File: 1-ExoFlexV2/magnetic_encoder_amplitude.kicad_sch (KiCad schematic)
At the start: 49 parts, among them J64 5,1k, J65 5,1k, J66 5,1k, J67 5,1k, J68 5,1k, J69 5,1k, U10 ADCMP602BRMZ, U11 SN74LVC1G32DBVR, U12 SN74LVC1G32DBVR, U8 ADCMP602BRMZ, U9 ADCMP602BRMZ

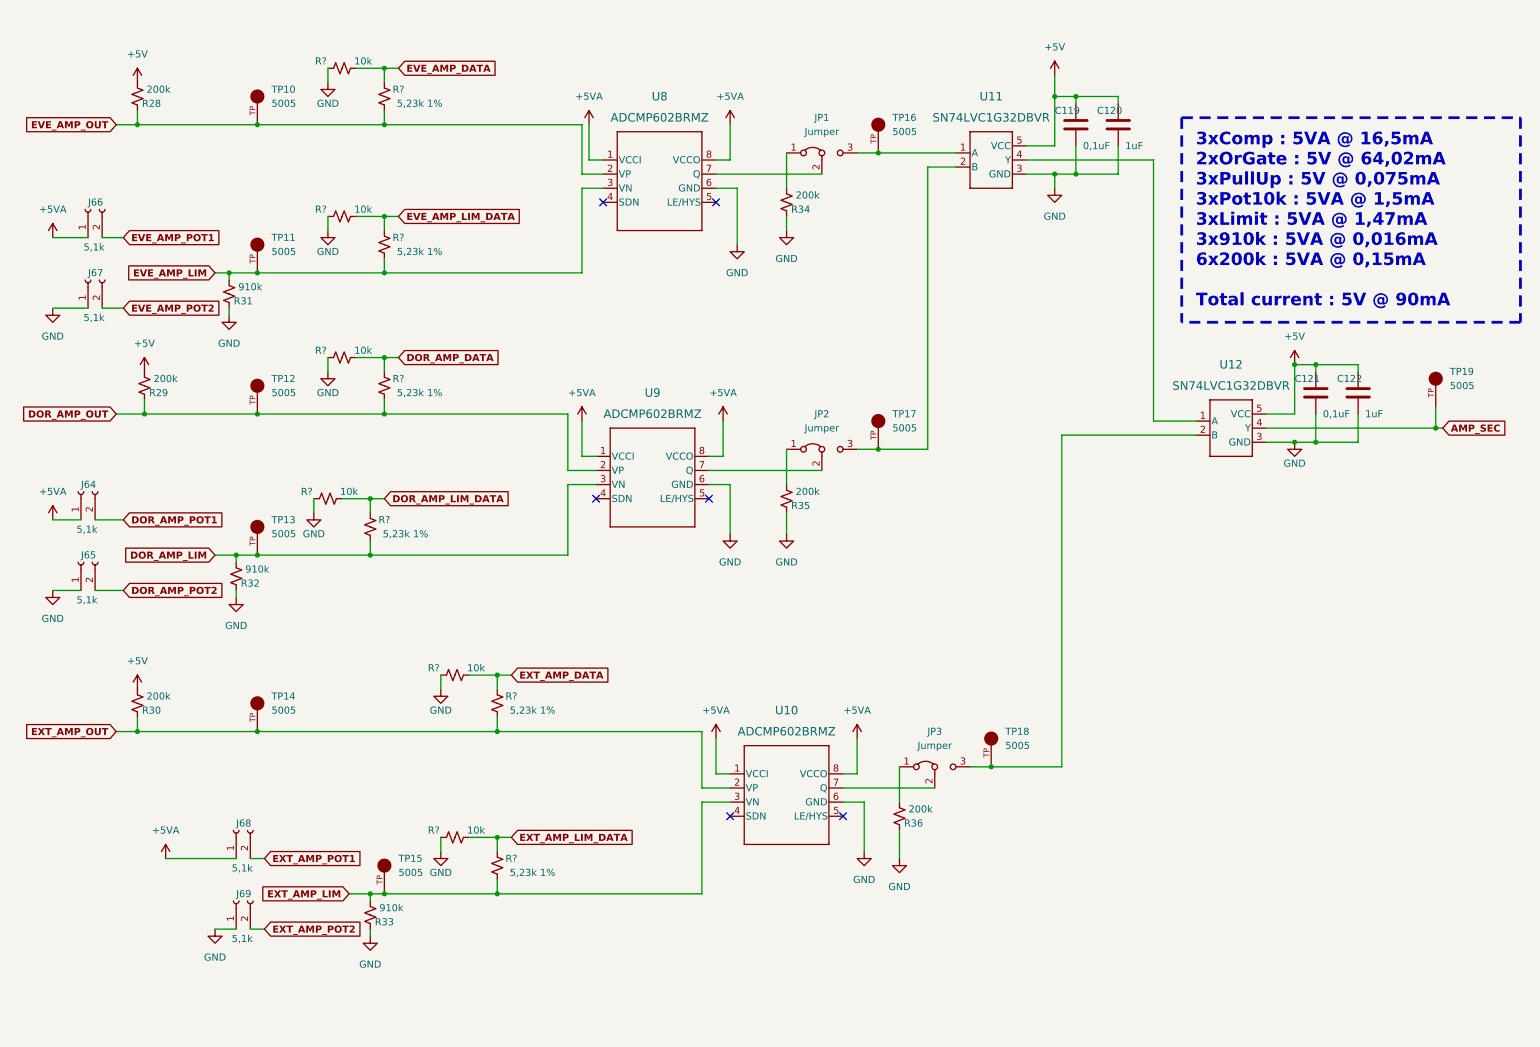
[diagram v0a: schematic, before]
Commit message: Finalisation 2
-Ajout des nouveaux comparateurs
- Ajout d'une page découplage
- Retrait des condensateur dans les autres pages
- Ajout de trimmer pour les résistance importante mais incertaines
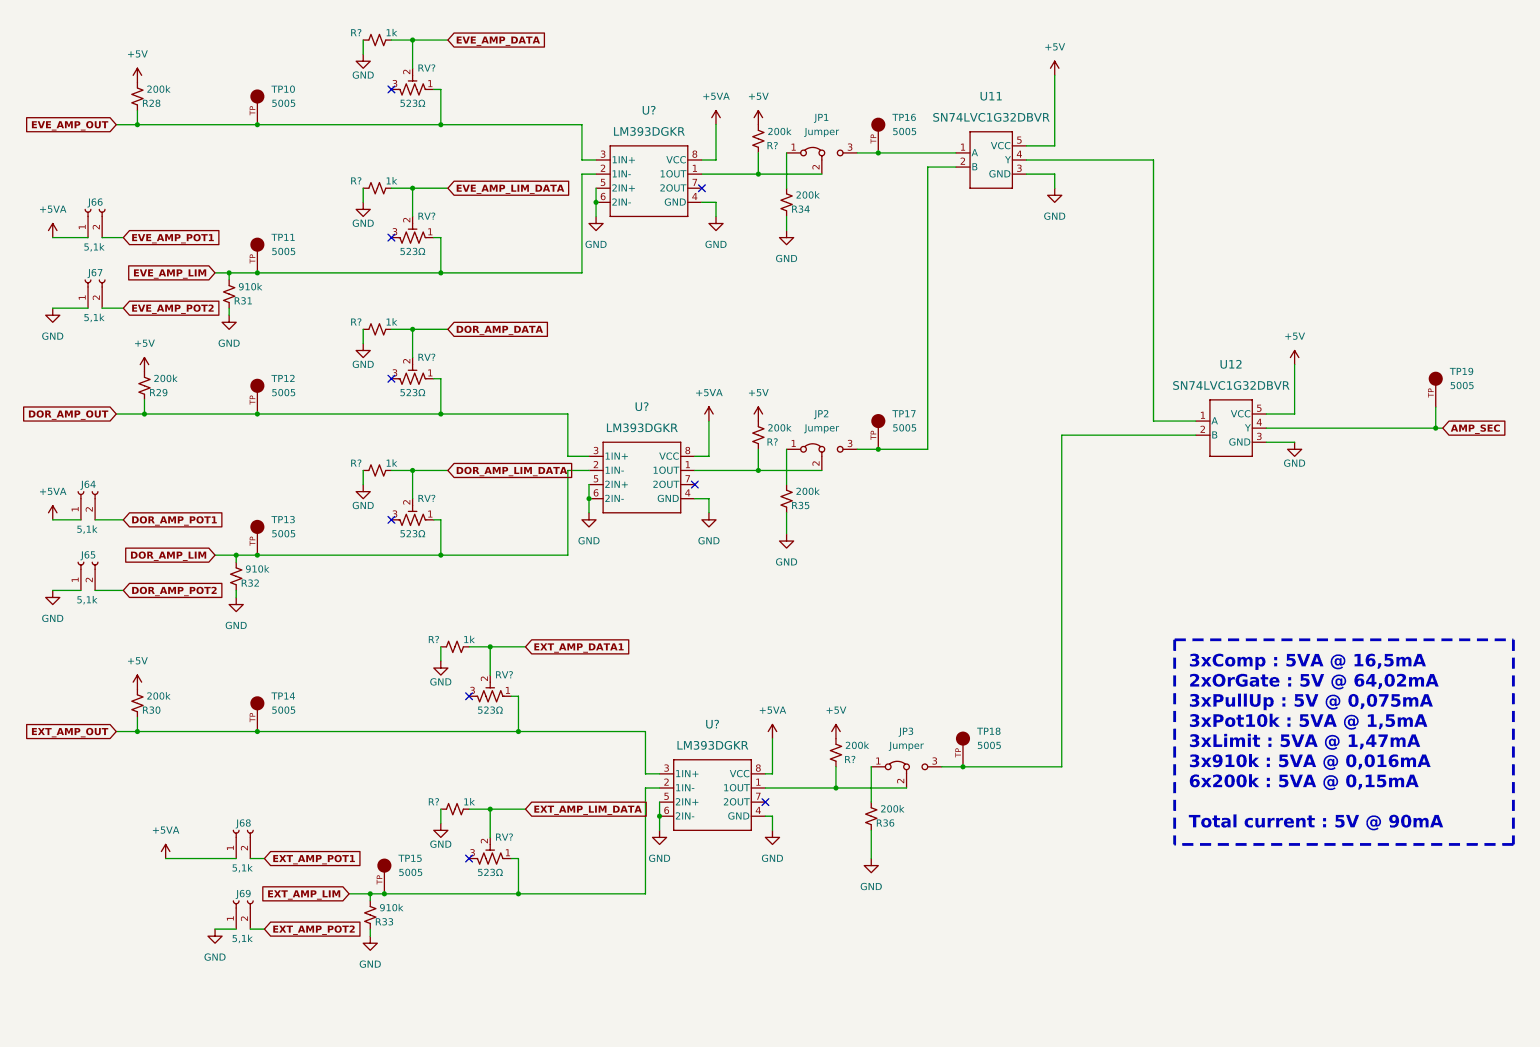
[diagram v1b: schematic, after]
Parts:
- removed C119, C121: 0,1uF, Capacitor_SMD:C_0603_1608Metric, symbol Device:C
- removed C120, C122: 1uF, Capacitor_SMD:C_0603_1608Metric, symbol Device:C
- removed R? (x6): 5,23k 1%, Resistor_SMD:R_0805_2012Metric, symbol Device:R_Small_US
- removed R? (x6): 10k, Resistor_SMD:R_0805_2012Metric, symbol Device:R_Small_US
- removed U10, U8, U9: ADCMP602BRMZ, FootPrint:ADCMP602BRMZ, symbol SymLib:ADCMP602BRMZ
- added R? (x3): 200k, Resistor_SMD:R_0603_1608Metric, symbol Device:R_Small_US
- added R? (x6): 1k, Resistor_SMD:R_0805_2012Metric, symbol Device:R_Small_US
- added RV? (x6): 523Ω, FootPrint:TRIM_3362P-1-102LF, symbol Device:R_Potentiometer_Trim_US
- added U? (x3): LM393DGKR, DGK8, symbol SymLib:LM393DGKR
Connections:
- net +5V: now also R?.1, R?.1, R?.1
- net +5VA: now also U?.8 (VCC), U?.8 (VCC), U?.8 (VCC)
- net DOR_AMP_DATA: now also R?.2, RV?.2
- net DOR_AMP_LIM: now also RV?.1, U?.2 (1IN-)
- net DOR_AMP_LIM_DATA: now also R?.2, RV?.2
- net DOR_AMP_OUT: now also RV?.1, U?.3 (1IN+)
- net EVE_AMP_DATA: now also R?.2, RV?.2
- net EVE_AMP_LIM: now also RV?.1, U?.2 (1IN-)
- net EVE_AMP_LIM_DATA: now also R?.2, RV?.2
- net EVE_AMP_OUT: now also RV?.1, U?.3 (1IN+)
- net EXT_AMP_LIM: now also RV?.1, U?.2 (1IN-)
- net EXT_AMP_LIM_DATA: now also R?.2, RV?.2
- net EXT_AMP_OUT: now also RV?.1, U?.3 (1IN+)
- net GND: now also R?.1, R?.1, R?.1, R?.1, R?.1, R?.1, U?.4 (GND), U?.4 (GND), U?.4 (GND), U?.5 (2IN+), U?.5 (2IN+), U?.5 (2IN+), U?.6 (2IN-), U?.6 (2IN-), U?.6 (2IN-)
- net at JP2.2 (C): now also R?.2, U?.1 (1OUT)
- net at JP1.2 (C): now also R?.2, U?.1 (1OUT)
- net at JP3.2 (C): now also R?.2, U?.1 (1OUT)
- new net EXT_AMP_DATA1: R?.2, RV?.2
- no-connect marks 6 -> 9
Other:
- moved on the sheet: JP3, R36, TP18

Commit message: Chokes et RC
- Ajout des RF chokes
- Changement des résistance pour 0805
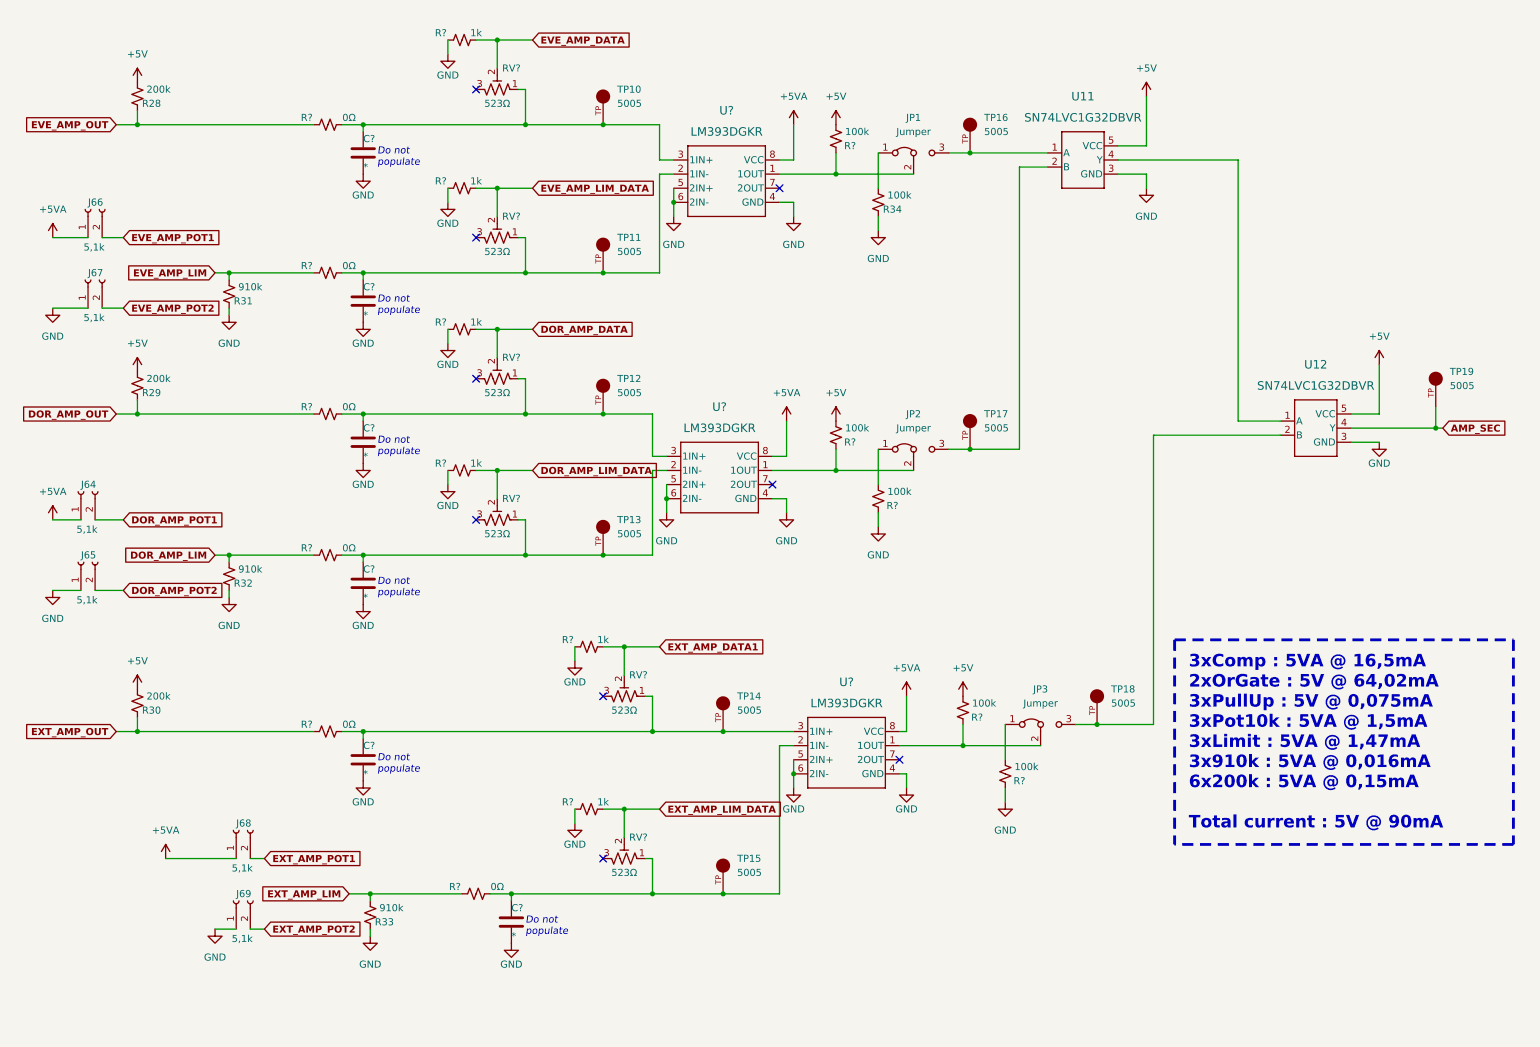
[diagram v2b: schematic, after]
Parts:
- removed R35, R36, R? (x2): 200k, Resistor_SMD:R_0603_1608Metric, symbol Device:R_Small_US
- added C? (x6): *, Capacitor_SMD:C_0805_2012Metric, symbol Device:C
- added R? (x4): 100k, Resistor_SMD:R_0805_2012Metric, symbol Device:R_Small_US
- added R? (x6): 0Ω, Resistor_SMD:R_0805_2012Metric, symbol Device:R_Small_US
- R28: footprint Resistor_SMD:R_0603_1608Metric -> Resistor_SMD:R_0805_2012Metric
- R34, R?: value 200k -> 100k; footprint Resistor_SMD:R_0603_1608Metric -> Resistor_SMD:R_0805_2012Metric
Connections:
- net +5V: now also R?.1, R?.1
- net DOR_AMP_LIM: now also R?.1; no longer RV?.1, TP13.TP, U?.2 (1IN-)
- net DOR_AMP_OUT: now also R?.1; no longer RV?.1, TP12.TP, U?.3 (1IN+)
- net EVE_AMP_LIM: now also R?.1; no longer RV?.1, TP11.TP, U?.2 (1IN-)
- net EVE_AMP_OUT: now also R?.1; no longer RV?.1, TP10.TP, U?.3 (1IN+)
- net EXT_AMP_LIM: now also R?.1; no longer RV?.1, TP15.TP, U?.2 (1IN-)
- net EXT_AMP_OUT: now also R?.1; no longer RV?.1, TP14.TP, U?.3 (1IN+)
- net GND: now also C?.2, C?.2, C?.2, C?.2, C?.2, C?.2, R?.2, R?.2
- net at JP3.2 (C), U?.1 (1OUT): now also R?.2
- net at JP2.1 (A): now also R?.1
- net at JP2.2 (C), U?.1 (1OUT): now also R?.2
- net at JP3.1 (A): now also R?.1
- new net: C?.1, R?.2, RV?.1, TP14.TP, U?.3 (1IN+)
- new net: C?.1, R?.2, RV?.1, TP10.TP, U?.3 (1IN+)
- new net: C?.1, R?.2, RV?.1, TP15.TP, U?.2 (1IN-)
- new net: C?.1, R?.2, RV?.1, TP13.TP, U?.2 (1IN-)
- new net: C?.1, R?.2, RV?.1, TP12.TP, U?.3 (1IN+)
- new net: C?.1, R?.2, RV?.1, TP11.TP, U?.2 (1IN-)
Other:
- note added: "Do not populate"
- moved on the sheet: JP1, JP2, JP3, R29, R32, R34, R?, RV?, TP10, TP11, TP12, TP13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

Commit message: Trimmer et jumper
-Changement de symbole de jumper
-Ajout des des trimmer aux endroits nécessaires
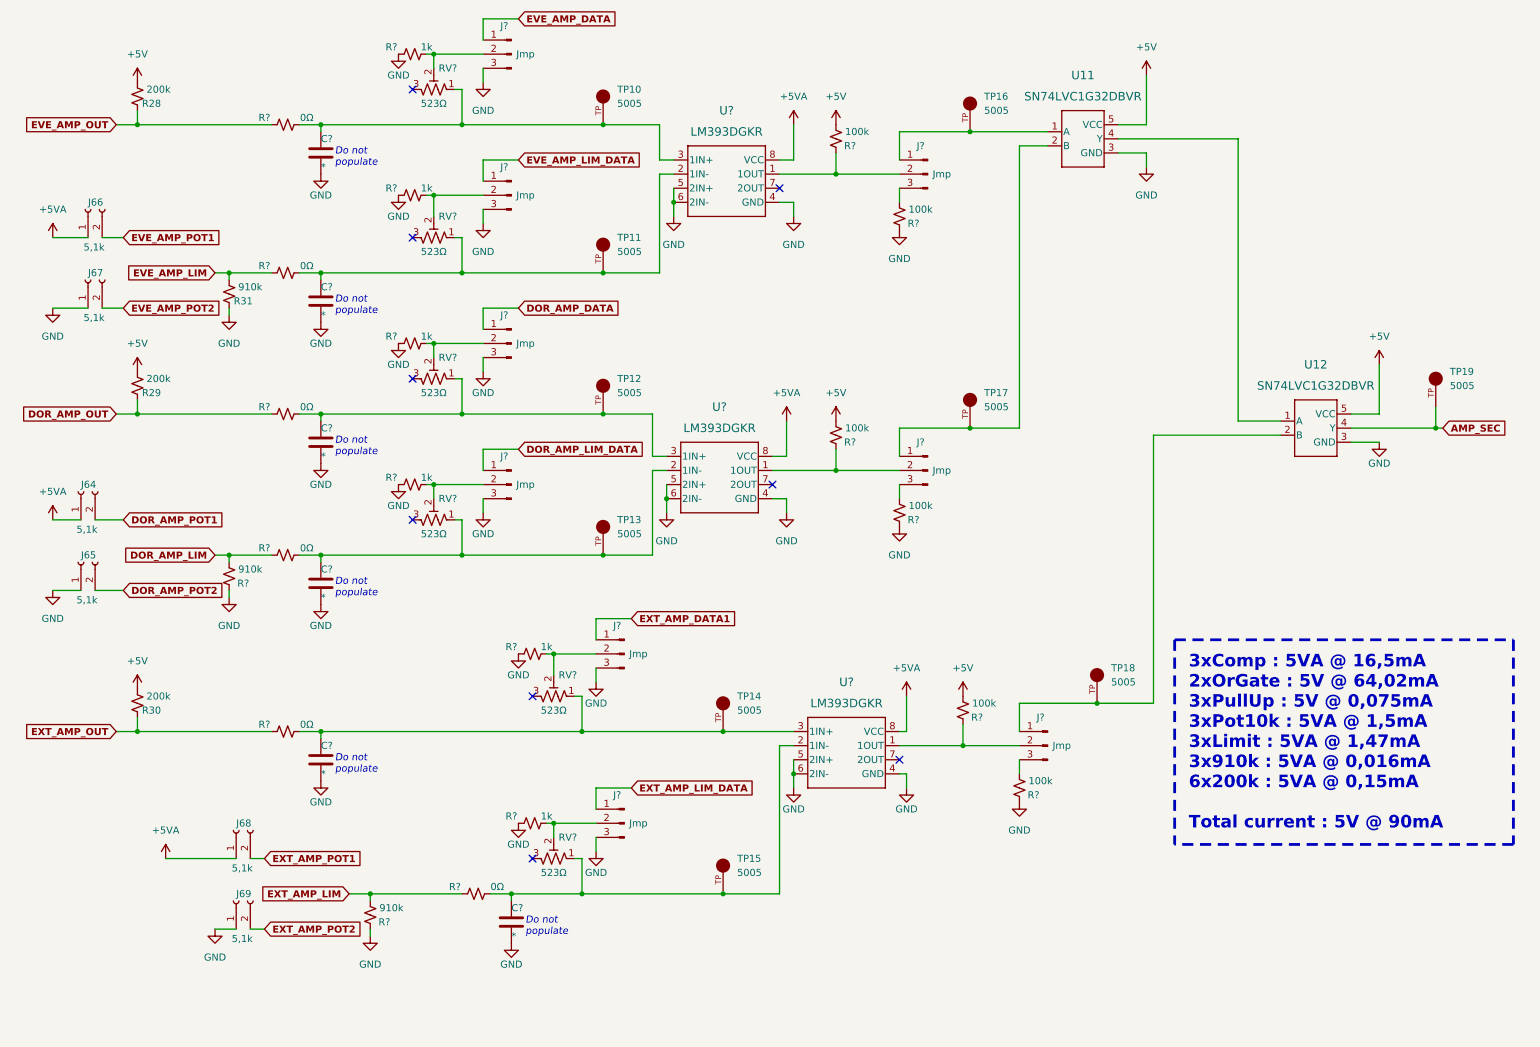
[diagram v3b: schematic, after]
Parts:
- removed JP1, JP2, JP3: Jumper, Connector_PinHeader_2.54mm:PinHeader_1x03_P2.54mm_Vertical, symbol Jumper:Jumper_3_Bridged12
- removed R32, R33: 910k, Resistor_SMD:R_0603_1608Metric, symbol Device:R_Small_US
- removed R34, R? (x2): 100k, Resistor_SMD:R_0805_2012Metric, symbol Device:R_Small_US
- added J? (x9): Jmp, symbol Connector:Conn_01x03_Male
- added R? (x3): 100k, Resistor_SMD:R_0805_2012Metric, symbol Device:R_Small_US
- added R? (x2): 910k, Resistor_SMD:R_0805_2012Metric, symbol Device:R_Small_US
- R31: footprint Resistor_SMD:R_0603_1608Metric -> Resistor_SMD:R_0805_2012Metric
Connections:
- net DOR_AMP_DATA: now also J?.1 (Pin_1); no longer R?.2, RV?.2
- net DOR_AMP_LIM: now also R?.1
- net DOR_AMP_LIM_DATA: now also J?.1 (Pin_1); no longer R?.2, RV?.2
- net EVE_AMP_DATA: now also J?.1 (Pin_1); no longer R?.2, RV?.2
- net EVE_AMP_LIM_DATA: now also J?.1 (Pin_1); no longer R?.2, RV?.2
- net EXT_AMP_DATA1: now also J?.1 (Pin_1); no longer R?.2, RV?.2
- net EXT_AMP_LIM: now also R?.1
- net EXT_AMP_LIM_DATA: now also J?.1 (Pin_1); no longer R?.2, RV?.2
- net GND: now also J?.3 (Pin_3), J?.3 (Pin_3), J?.3 (Pin_3), J?.3 (Pin_3), J?.3 (Pin_3), J?.3 (Pin_3), R?.2, R?.2, R?.2, R?.2, R?.2
- net at TP18.TP, U12.2 (B): now also J?.1 (Pin_1)
- net at R?.2, U?.1 (1OUT): now also J?.2 (Pin_2) (x3)
- net at TP17.TP, U11.2 (B): now also J?.1 (Pin_1)
- net at TP16.TP, U11.1 (A): now also J?.1 (Pin_1)
- new net: J?.2 (Pin_2), R?.2, RV?.2 (x6)
- new net: J?.3 (Pin_3), R?.1 (x3)
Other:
- moved on the sheet: C?, R?, RV?, TP16, TP17, TP18, U11
